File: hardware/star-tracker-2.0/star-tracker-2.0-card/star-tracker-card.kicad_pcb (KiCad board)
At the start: 4 copper layers, 99.8 x 94.6 mm, 225 parts, among them J1 TFM-120-01-L-D-RA, J2 SM14B-SHLS-TF, J3 GRPB041VWVN-RC, J4 3-2492104-6, J5 DM3BT-DSF-PEJS, J6 Conn_01x02, Q1 DMP2240UDM, Q2 DMN3028LQ-7, Q3 DMP3050LVT-7, Q4 DMP3050LVT-7, Q5 DMN3028LQ-7, Q6 MMBT2907, U1 MAX7310ATE, U10 RCLAMP0504FB, U11 ICM-42688-P, U12 TCAN330, U13 EMMC+RESET+5.1-COMPATIBLE-BA, U14 TCA9509DGKRDGK8-M, U15 CLVCH16T245MDGGREP, U16 SN74LVC8T245MPWREPPW24-M, U17 TLV70028QDDCRQ1, U2 MIC842LYC5, U3 MIC842LYC5, U4 TPS62112, U5 TS5A21366DCUR, U6 MAX4211FETE, U7 OSD3358-512M-BSM, U8 SN74LVC1G07DCK, U9 TLVH431, Y1 ECS-240-12-30BQ-AEN-TR, Y2 ABS07-32.768KHZ-T

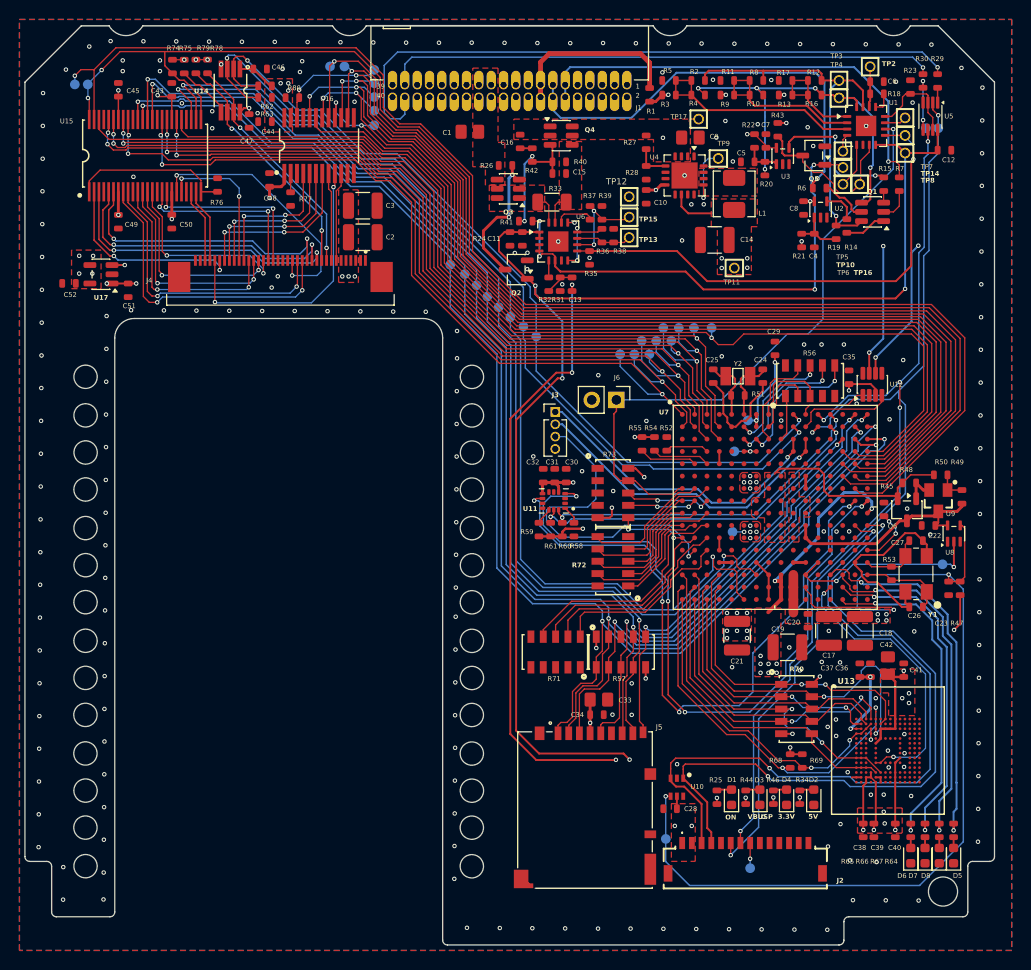
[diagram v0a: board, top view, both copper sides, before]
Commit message: Minor PCB changes
updated description of component in BOM, changed filet radius on polygon pours, changed PCB footprint to Star tracker 2.0 PCB. Added more ground vias.
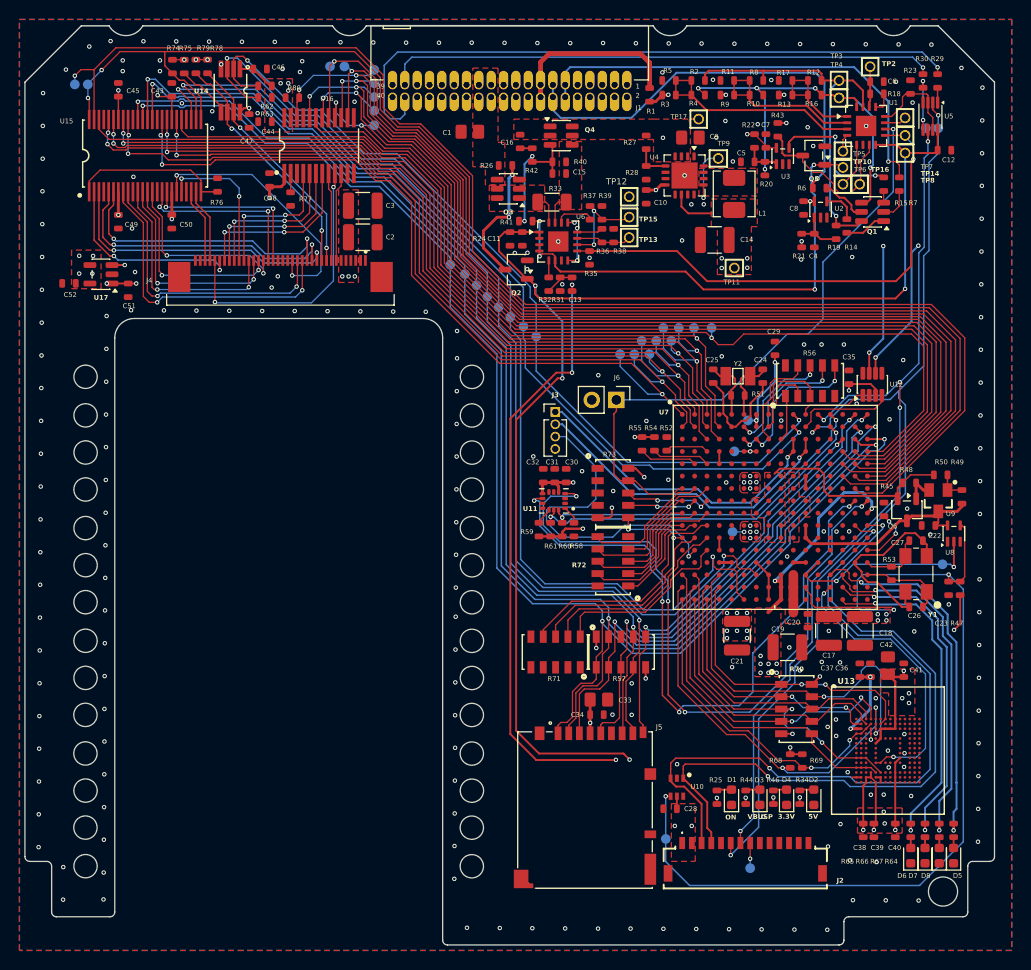
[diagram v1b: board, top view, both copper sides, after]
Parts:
- removed U$3: , star-tracker-card:PSAS_LOGO_10X10
- PCB1: value ORESAT-CARD-V1.3-STAR-TRACKER -> ORESAT-CARD-V2.0-STAR-TRACKER; footprint star-tracker-card:ORESAT-CARD-V1.3-STAR-TRACKER -> oresat-pcbs:ORESAT-CARD-V2.0-STAR-TRACKER
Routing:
- net GND: vias 229 -> 237
